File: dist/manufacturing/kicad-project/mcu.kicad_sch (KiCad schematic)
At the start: 33 parts, among them J4 B6B-PH-K-S(LF)(SN), SW1 SW1, U16 STM32G0B1CBT6, U17 W25Q32JVSSIQ, Y1 16MHz / 9pF

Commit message: Complete orderable PD1180-EPR board release
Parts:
- removed GND (x9): GND, symbol Custom:rail_down
- removed J4: B6B-PH-K-S(LF)(SN), symbol Device:J_B6B-PH-K-S_LF_SN
- removed SW1: SW1, symbol Device:push_button_normally_open_momentary_right
- removed V3V3 (x7): V3V3, symbol Custom:rail_up
- added GND (x10): GND, symbol Custom:rail_down
- added SW1: SW1, symbol Device:push_button_normally_open_momentary_down
- added TP_NRST: TP_NRST, symbol Device:testpoint_right
- added TP_STATUS: TP_STATUS, symbol Device:testpoint_right
- added TP_SWCLK: TP_SWCLK, symbol Device:testpoint_right
- added TP_SWDIO: TP_SWDIO, symbol Device:testpoint_right
- added TP_SWD_3V3: TP_SWD_3V3, symbol Device:testpoint_right
- added TP_SWD_GND: TP_SWD_GND, symbol Device:testpoint_right
- added V3V3 (x8): V3V3, symbol Custom:rail_up
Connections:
- net at U16.10 (PF2_NRST): now also TP_NRST.1
- net at U16.4 (VBAT), U16.5 (VREF_POS), U16.6 (VDD): now also V3V3.1
- net at C48.2, U16.7 (VSS): now also GND.1
- net at Y1.2: now also GND.1
- net at Y1.4: now also GND.1
- net at C44.1, C45.1, C46.1: now also V3V3.1; no longer C47.1
- net at C44.2, C45.2, C46.2: now also GND.1; no longer C47.2
- net at U17.7 (HOLD__or_RESET__IO3), U17.8 (VCC): now also V3V3.1
- net at U17.1 (N_CS): now also R73.2
- net at U17.3 (WP__IO2): now also V3V3.1
- net at C51.2, U17.4 (GND): now also GND.1
- net at C51.1, R73.1: now also V3V3.1
- net at C50.2: now also GND.1
- net at R70.1: now also V3V3.1
- net at C49.2: now also GND.1
- new net: GND.1, TP_SWD_GND.1
- new net: TP_SWD_3V3.1, V3V3.1
- new net: C47.2, GND.1
- new net: C47.1, V3V3.1
- new net: GND.1, SW1.2
- new net STATUS_GPIO: TP_STATUS.1
- new net SWDIO: TP_SWDIO.1
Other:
- note added: "U16: system MCU with native USB, FDCAN and ADC monitoring. U17: 32 Mbit external SPI configuration/telemetry flash."
- note added: "USB_DATA_VBUS_SENSE"

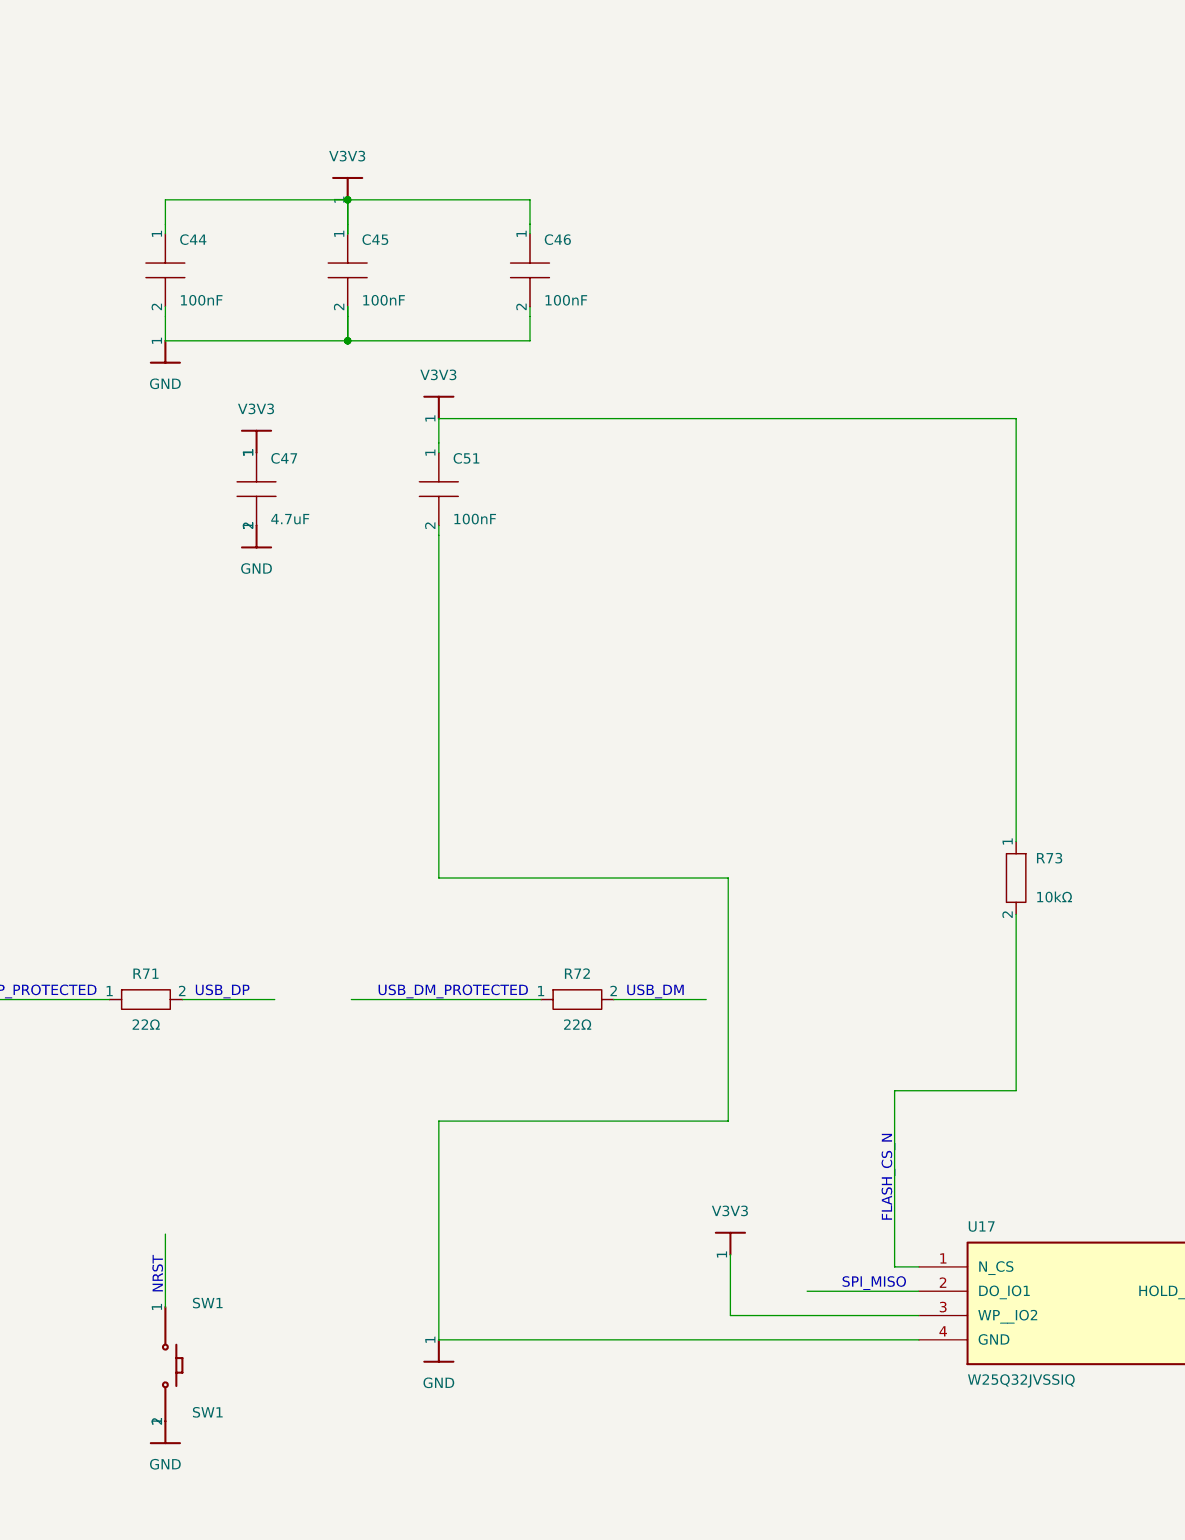
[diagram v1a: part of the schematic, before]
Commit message: Fix schematic style and top-side reset switch
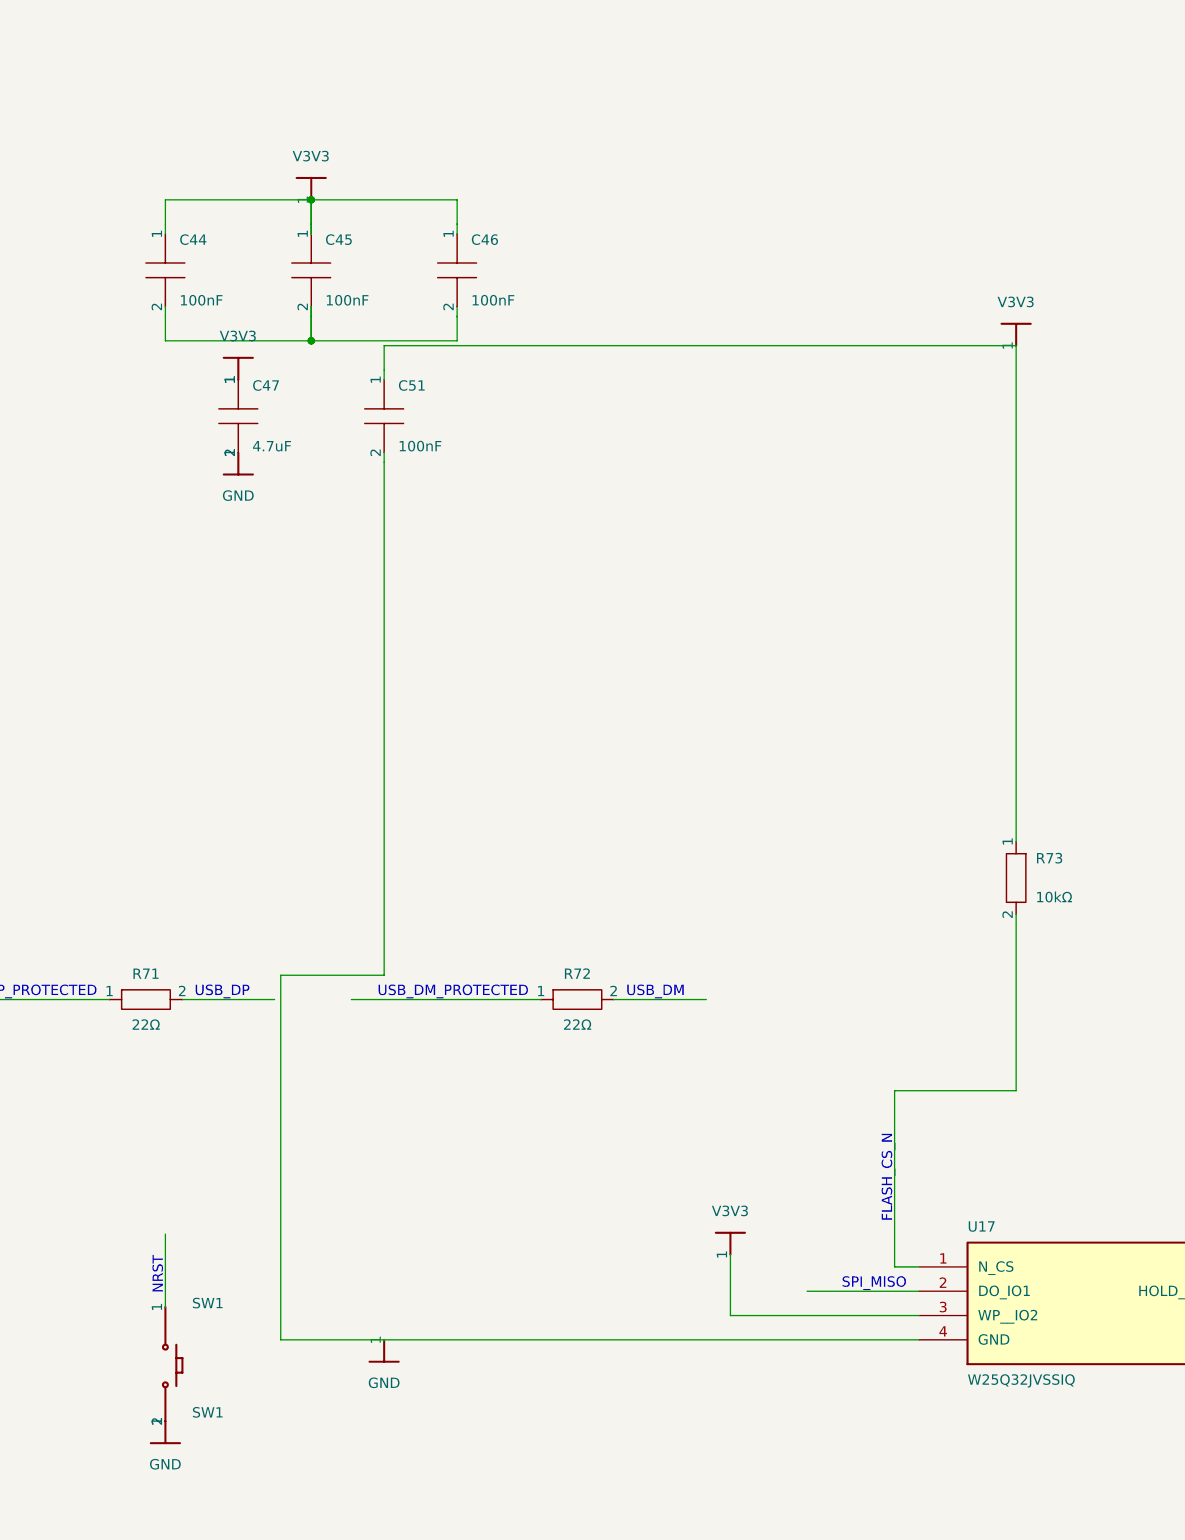
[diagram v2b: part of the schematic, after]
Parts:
- removed GND (x10): GND, symbol Custom:rail_down
- removed V3V3 (x8): V3V3, symbol Custom:rail_up
- added GND (x9): GND, symbol Custom:rail_down
- added V3V3 (x8): V3V3, symbol Custom:rail_up
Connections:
- net at R70.1: now also V3V3.1
- net at U17.3 (WP__IO2): now also V3V3.1
- net at U17.7 (HOLD__or_RESET__IO3), U17.8 (VCC): now also V3V3.1
- net at TP_SWD_GND.1: now also GND.1
- net at C44.1, C45.1, C46.1: now also V3V3.1
- net at TP_SWD_3V3.1: now also V3V3.1
- net at C49.2: now also GND.1
- net at Y1.2: now also GND.1
- net at Y1.4: now also GND.1
- net at C50.2: now also GND.1
- net at C47.2: now also GND.1
- net at C47.1: now also V3V3.1
- net at SW1.2: now also GND.1
- net at C51.1, R73.1: now also V3V3.1
- net at C48.2, U16.7 (VSS): now also GND.1
- net at U16.4 (VBAT), U16.5 (VREF_POS), U16.6 (VDD): now also V3V3.1

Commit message: Use one USB-C port for PD and data
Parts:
- removed GND (x9): GND, symbol Custom:rail_down
- removed V3V3 (x8): V3V3, symbol Custom:rail_up
- added GND (x9): GND, symbol Custom:rail_down
- added V3V3 (x8): V3V3, symbol Custom:rail_up
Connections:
- net at C47.2: now also GND.1
- net at C44.1, C45.1, C46.1: now also V3V3.1
- net at C47.1: now also V3V3.1
- net at TP_SWD_3V3.1: now also V3V3.1
- net at U17.3 (WP__IO2): now also V3V3.1
- net at U17.7 (HOLD__or_RESET__IO3), U17.8 (VCC): now also V3V3.1
- net at U16.4 (VBAT), U16.5 (VREF_POS), U16.6 (VDD): now also V3V3.1
- net at C48.2, U16.7 (VSS): now also GND.1
- net at C50.2: now also GND.1
- net at R70.1: now also V3V3.1
- net at C49.2: now also GND.1
- net at SW1.2: now also GND.1
- net at Y1.2: now also GND.1
- net at Y1.4: now also GND.1
- net at TP_SWD_GND.1: now also GND.1
- net at C51.1, R73.1: now also V3V3.1
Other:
- note added: "USB_VBUS_SENSE"
- note removed: "USB_DATA_VBUS_SENSE"

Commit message: fix: finalize single-port EPR controller
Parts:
- removed GND (x9): GND, symbol Custom:rail_down
- removed V3V3 (x8): V3V3, symbol Custom:rail_up
- C44, C45, C46, C48, C49, C50, C51: footprint (none) -> capacitor_cap0603
- C47: footprint (none) -> capacitor_cap1206
- R70, R71, R72, R73: footprint (none) -> resistor_res0603
- SW1: footprint (none) -> TS-1088-AR02016
- TP_NRST, TP_STATUS, TP_SWCLK, TP_SWDIO, TP_SWD_3V3, TP_SWD_GND: footprint (none) -> test_point
- U16: footprint (none) -> STM32G0B1CBT6
- U17: footprint (none) -> W25Q32JVSSIQ
- Y1: value 16MHz / 9pF -> Y1; footprint (none) -> X322516MLB4SI
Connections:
- net STATUS_GPIO: now also U16.1 (PC13)
- net SWDIO: now also U16.35 (PA13)
- net NRST: now reaches C48.1, R70.2
- net NRST: now also SW1.1, TP_NRST.1, U16.10 (PF2_NRST)
- net GND: now reaches C48.2, U16.7 (VSS)
- net GND: now also C44.2, C45.2, C46.2, C47.2, C49.2, C50.2, C51.2, SW1.2, TP_SWD_GND.1, U17.4 (GND), Y1.2, Y1.4
- net V3V3: now reaches C47.1
- net V3V3: now also C44.1, C45.1, C46.1, C51.1, R70.1, R73.1, TP_SWD_3V3.1, U16.4 (VBAT), U16.5 (VREF_POS), U16.6 (VDD), U17.3 (WP__IO2), U17.7 (HOLD__or_RESET__IO3), U17.8 (VCC)
- net OSC_IN: now reaches C49.1, Y1.1
- net OSC_IN: now also U16.8 (PF0_OSC_IN)
- net OSC_OUT: now reaches C50.1, Y1.3
- net OSC_OUT: now also U16.9 (PF1_OSC_OUT)
- net SWCLK: now reaches TP_SWCLK.1
- net SWCLK: now also U16.36 (PA14_BOOT0)
- net VMON_ADC: now reaches U16.11 (PA0)
- net IIN_MON: now reaches U16.12 (PA1)
- net RS485_TX: now reaches U16.13 (PA2)
- net RS485_RX: now reaches U16.14 (PA3)
- net TMC_CS_N: now reaches U16.15 (PA4)
- net SPI_SCK: now reaches U16.16 (PA5)
- net SPI_SCK: now also U17.6 (CLK)
- net SPI_MISO: now reaches U16.17 (PA6)
- net SPI_MISO: now also U17.2 (DO_IO1)
- net SPI_MOSI: now reaches U16.18 (PA7)
- net SPI_MOSI: now also U17.5 (DI_IO0)
- net USB_VBUS_SENSE: now reaches U16.19 (PB0)
- net DIN0: now reaches U16.2 (PC14_OSC32_IN)
- net PD_IRQ_N: now reaches U16.20 (PB1)
- net EFUSE_FAULT_N: now reaches U16.21 (PB2)
- net RS485_DE: now reaches U16.22 (PB10)
- net ENC_CS_N: now reaches U16.23 (PB11)
- net FLASH_CS_N: now reaches U16.24 (PB12)
- net FLASH_CS_N: now also R73.2, U17.1 (N_CS)
- net STOP_L: now reaches U16.25 (PB13)
- net STOP_R: now reaches U16.26 (PB14)
- net HOME_IN: now reaches U16.27 (PB15)
- net SD_MODE: now reaches U16.28 (PA8)
- net RS232_TX: now reaches U16.29 (PA9)
- net DIN1: now reaches U16.3 (PC15_OSC32_OUT)
- net STEP_IN: now reaches U16.30 (PC6)
- net DIR_IN: now reaches U16.31 (PC7)
- net RS232_RX: now reaches U16.32 (PA10)
- net USB_DM: now reaches U16.33 (PA11_PA9_)
- net USB_DM: now also R72.2
- net USB_DP: now reaches U16.34 (PA12_PA10_)
- net USB_DP: now also R71.2
- net MCU_RUN: now reaches U16.37 (PA15)
- net CAN_RX: now reaches U16.38 (PD0)
- net CAN_TX: now reaches U16.39 (PD1)
- net OUT0_DRIVE: now reaches U16.40 (PD2)
- net OUT1_DRIVE: now reaches U16.41 (PD3)
- net TMC_DIAG0: now reaches U16.42 (PB3)
- net MOTOR_PG: now reaches U16.43 (PB4)
- net POWER_PERMIT: now reaches U16.44 (PB5)
- net PD_SCL: now reaches U16.45 (PB6)
- net PD_SDA: now reaches U16.46 (PB7)
- net TMC_DIAG1: now reaches U16.47 (PB8)
- net VMOTOR_OK: now reaches U16.48 (PB9)
- net USB_DP_PROTECTED: now reaches R71.1
- net USB_DM_PROTECTED: now reaches R72.1
